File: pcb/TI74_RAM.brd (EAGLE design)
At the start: 25.4 x 27 mm, 10 parts, among them IC1 JEDEC_32KB_SRAM, X1 TI74_CONNREG

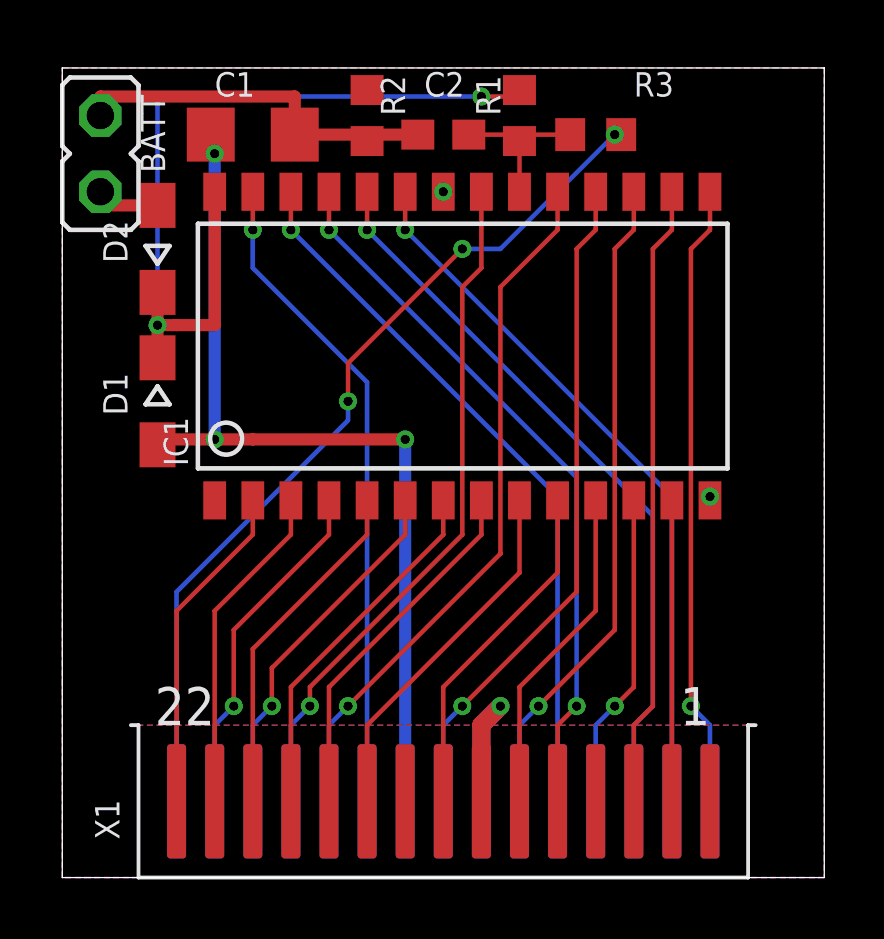
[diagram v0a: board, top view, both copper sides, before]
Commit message: Add in A14 address line
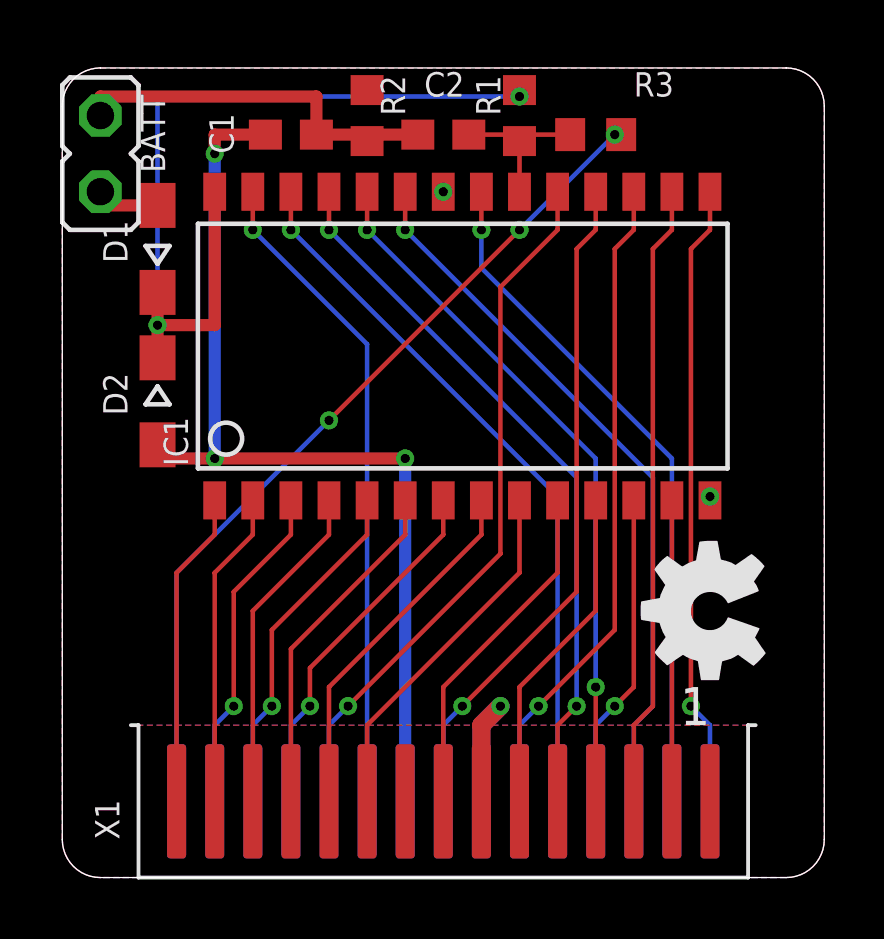
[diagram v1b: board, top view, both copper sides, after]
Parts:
- added GOLD_ORB_SM1: Open Source Hardware, oshw:OSHW_5MM
- C1: value 100 -> 100n; device resistor:C1206 -> resistor:C0603
- C2: value 1 -> 1n
- moved D1 5.08 mm to (-9.53, 21.0), turned to 90 degrees
- moved D2 5.08 mm to (-9.53, 15.9), turned to 270 degrees
- moved C1 1.27 mm to (-5.08, 24.8)
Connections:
- net A1: now also IC1.3; no longer IC1.4
- net A10: now also IC1.6; no longer IC1.7
- net A14: now also IC1.24
- net A2: now also IC1.4; no longer IC1.5
- net A4: now also IC1.21; no longer IC1.23
- net A5: now also IC1.23; no longer IC1.24
- net A6: now also IC1.5; no longer IC1.6
- net A7: now also IC1.7; no longer IC1.21
- net A8: now also IC1.1; no longer IC1.2
- net A9: now also IC1.2; no longer IC1.3
- net GND: no longer IC1.1
- net N$2: now also D2.A; no longer D1.A
- net N$3: now also D1.A; no longer D2.A
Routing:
- net A14: track 0.00 -> 23.5 mm, vias 0 -> 2
- net A7: track 23.0 -> 12.1 mm
- net N$2: track 30.8 -> 32.8 mm
- net A4: track 24.0 -> 23.0 mm
- net !CS2: track 29.2 -> 28.5 mm
- net A9: track 11.1 -> 10.6 mm
- net A8: track 11.1 -> 10.6 mm
- net A6: track 12.1 -> 11.6 mm
- net A5: track 24.5 -> 24.0 mm
- net A2: track 11.6 -> 11.1 mm
- net A10: track 12.1 -> 11.6 mm
- net A1: track 11.6 -> 11.1 mm
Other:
- outline, holes or cut-outs redrawn
